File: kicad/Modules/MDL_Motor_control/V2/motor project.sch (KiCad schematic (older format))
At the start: 4 parts

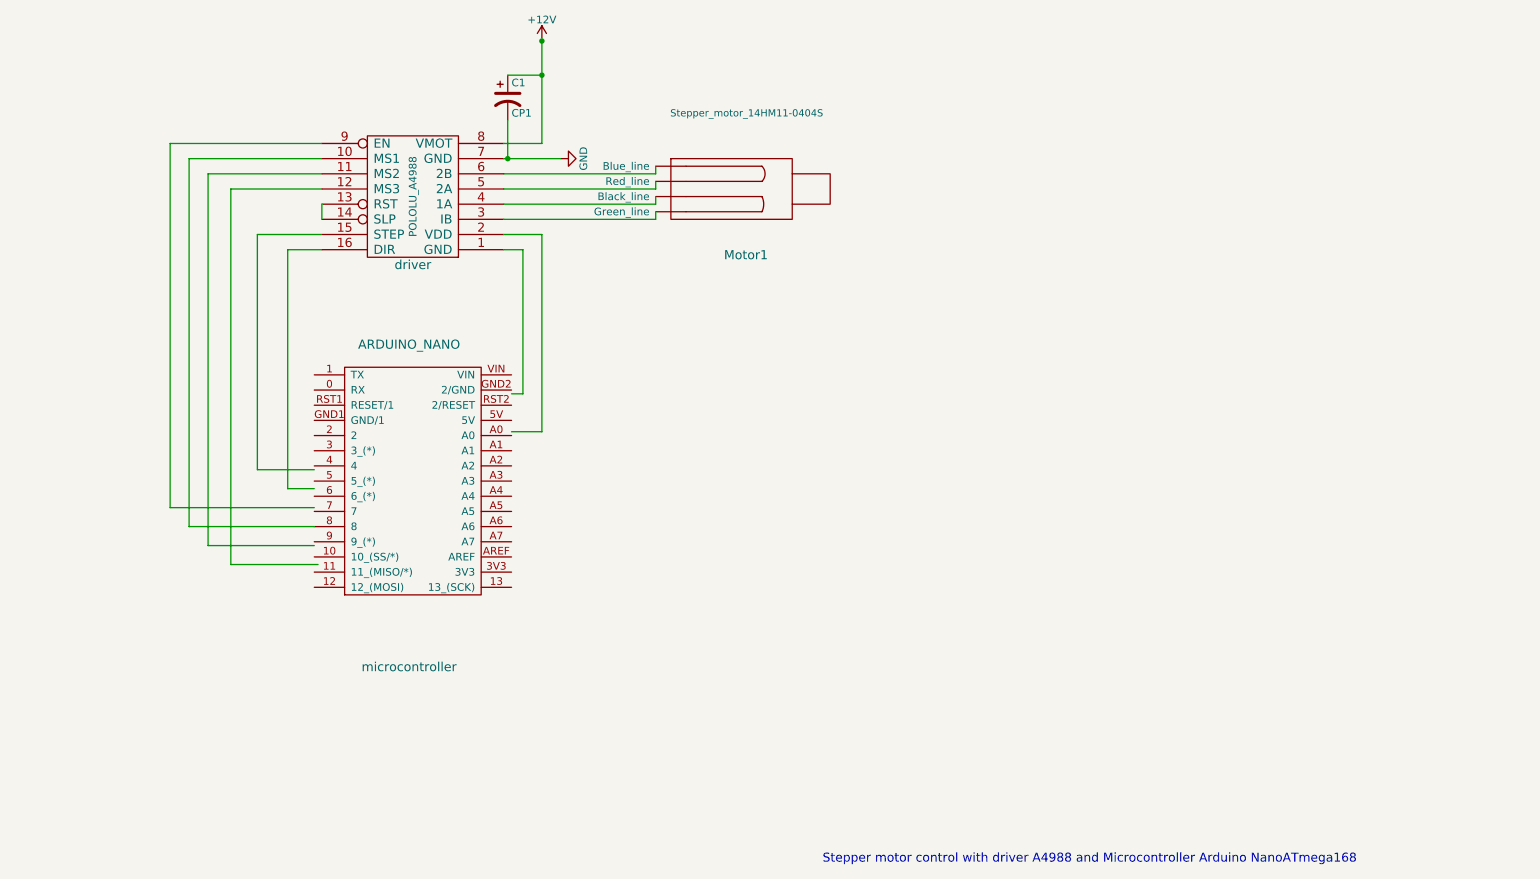
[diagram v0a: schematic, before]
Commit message: adding software modules (flowcharts)
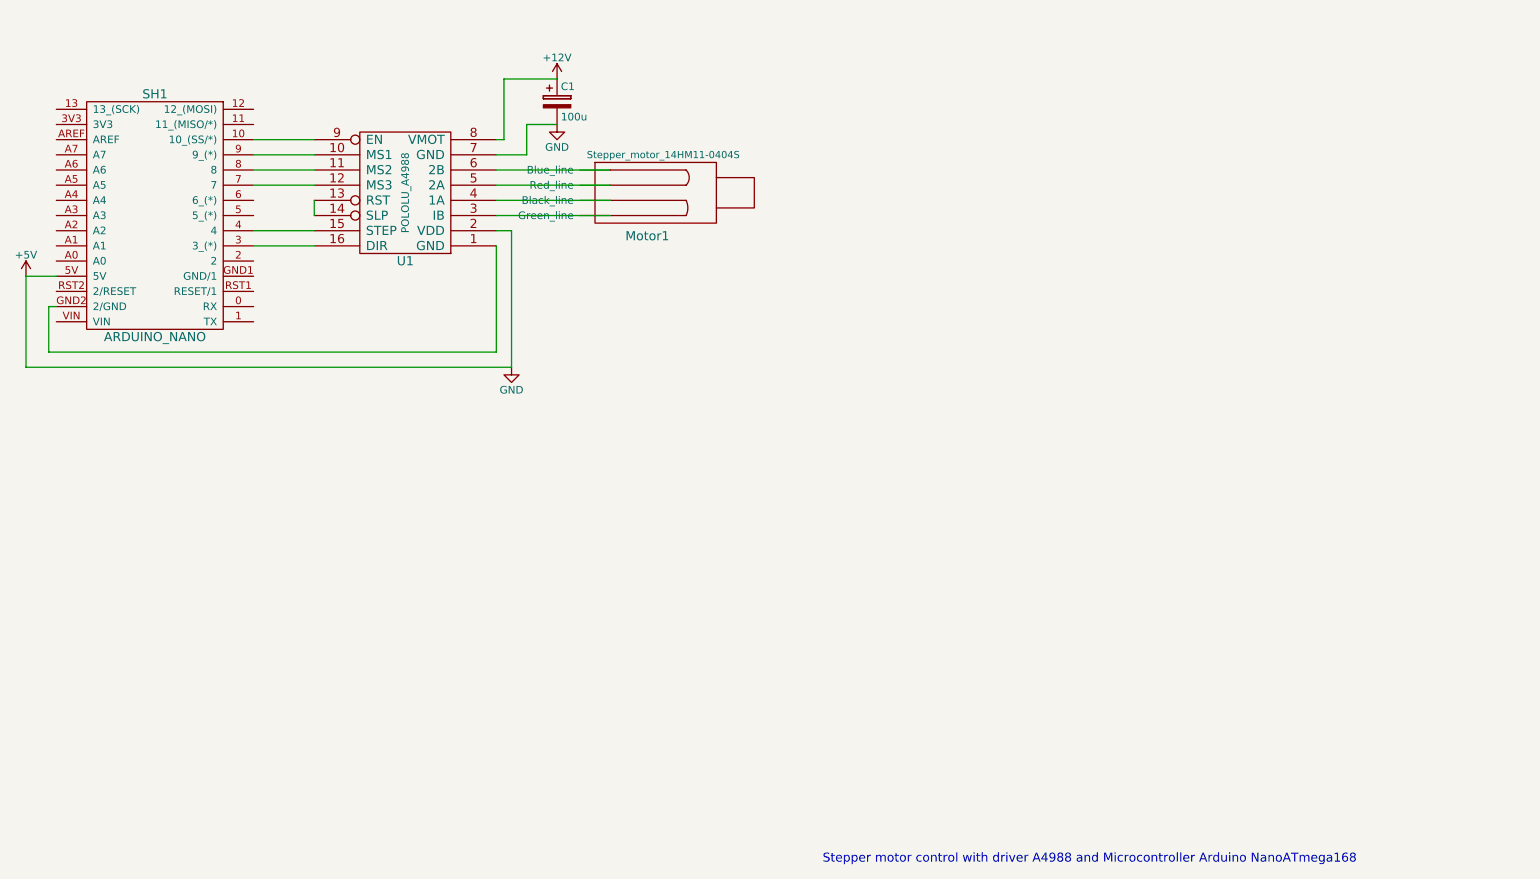
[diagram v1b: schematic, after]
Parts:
- removed C1: CP1, symbol CP1
- removed driver: POLOLU_A4988, symbol POLOLU_A4988
- removed microcontroller: ARDUINO_NANO, symbol ARDUINO_NANO
- added C1: 100u, symbol CP
- added SH1: ARDUINO_NANO, symbol ARDUINO_NANO
- added U1: POLOLU_A4988, symbol POLOLU_A4988
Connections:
- net labels added: +5V
- wire segments 38 -> 26
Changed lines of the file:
@@
 EESchema Schematic File Version 2
-LIBS:pololu_a4988
 LIBS:power
 LIBS:device
@@
 LIBS:contrib
 LIBS:valves
-LIBS:arduino
-LIBS:shield_arduino
-LIBS:stepper_motor_14hm11-0404s
-LIBS:projet moteur-cache
+LIBS:echopen
+LIBS:motor project-cache
 EELAYER 25 0
 EELAYER END
@@
 Comment4 ""
 $EndDescr
+Text Notes 7300 7475 0    59   ~ 0
+Stepper motor control with driver A4988 and Microcontroller Arduino NanoATmega168
 $Comp
-L POLOLU_A4988 driver
-U 1 1 577B8019
-P 4600 3075
-F 0 "driver" H 4600 3525 60  0000 C CNN
-F 1 "POLOLU_A4988" V 4600 3075 50  0000 C CNN
-F 2 "" H 4600 3075 60  0000 C CNN
-F 3 "" H 4600 3075 60  0000 C CNN
-	1    4600 3075
+L POLOLU_A4988 U1
+U 1 1 57A99E63
+P 4550 3050
+F 0 "U1" H 4550 3500 60  0000 C CNN
+F 1 "POLOLU_A4988" V 4550 3050 50  0000 C CNN
+F 2 "" H 4550 3050 60  0000 C CNN
+F 3 "" H 4550 3050 60  0000 C CNN
+	1    4550 3050
 	-1   0    0    1
 $EndComp
 $Comp
-L ARDUINO_NANO microcontroller
-U 1 1 577B8A9A
-P 4600 5100
-F 0 "microcontroller" H 4575 4025 60  0000 C CNN
-F 1 "ARDUINO_NANO" H 4575 6150 60  0000 C CNN
-F 2 "" H 3675 4500 60  0000 C CNN
-F 3 "" H 3675 4500 60  0000 C CNN
-	1    4600 5100
+L ARDUINO_NANO SH1
+U 1 1 57A9ABD4
+P 2900 3050
+F 0 "SH1" H 2900 2400 60  0000 C CNN
+F 1 "ARDUINO_NANO" H 2900 4000 60  0000 C CNN
+F 2 "" H 1975 2450 60  0000 C CNN
+F 3 "" H 1975 2450 60  0000 C CNN
+	1    2900 3050
+	-1   0    0    1
+$EndComp
+$Comp
+L Stepper_motor_14HM11-0404S Motor1
+U 1 1 57A9AFD6
+P 6500 3700
+F 0 "Motor1" H 6000 4100 60  0000 L TNN
+F 1 "Stepper_motor_14HM11-0404S" H 6250 4600 47  0000 C CNN
+F 2 "" H 5800 3600 60  0000 C CNN
+F 3 "" H 5400 5200 60  0000 C CNN
+	1    6500 3700
 	1    0    0    -1
 $EndComp
 Wire Wire Line
-	4000 3425 3775 3425
+	5150 3200 5900 3200
 Wire Wire Line
-	3775 3425 3775 5000
+	5150 3100 5900 3100
 Wire Wire Line
-	3775 5000 3950 5000
+	5150 3000 5900 3000
 Wire Wire Line
-	4000 3325 3575 3325
-Wire Wire Line
-	3575 3325 3575 4875
-Wire Wire Line
-	3575 4875 3950 4875
-Wire Wire Line
-	4000 3225 4000 3125
-Wire Wire Line
-	3400 3025 3400 5500
-Wire Wire Line
-	3400 5500 3975 5500
-Wire Wire Line
-	3250 2925 3250 5375
-Wire Wire Line
-	3125 2825 3125 5250
-Wire Wire Line
-	3000 2725 3000 5125
-Wire Wire Line
-	3000 5125 3950 5125
-Wire Wire Line
-	5200 3425 5325 3425
-Wire Wire Line
-	5325 3425 5325 4375
-Wire Wire Line
-	5325 4375 5250 4375
-Wire Wire Line
-	5200 3325 5450 3325
-Wire Wire Line
-	5450 3325 5450 4625
-Wire Wire Line
-	5450 4625 5250 4625
-Wire Wire Line
-	5200 2925 6200 2925
-Wire Wire Line
-	5200 3125 6200 3125
-Wire Wire Line
-	5200 3225 6200 3225
-Wire Wire Line
-	5200 3025 6200 3025
-Wire Wire Line
-	3125 5250 3950 5250
-Wire Wire Line
-	3250 5375 3950 5375
-Wire Wire Line
-	3400 3025 4000 3025
-Wire Wire Line
-	3250 2925 4000 2925
-Wire Wire Line
-	3125 2825 4000 2825
-Wire Wire Line
-	3000 2725 4000 2725
+	5150 2900 5900 2900
 $Comp
-L +12V #PWR?
-U 1 1 577BC707
-P 5450 2050
-F 0 "#PWR?" H 5450 1900 50  0001 C CNN
-F 1 "+12V" H 5450 2190 50  0000 C CNN
-F 2 "" H 5450 2050 50  0000 C CNN
-F 3 "" H 5450 2050 50  0000 C CNN
-	1    5450 2050
+L CP C1
+U 1 1 57A9B39D
+P 5550 2450
+F 0 "C1" H 5575 2550 50  0000 L CNN
+F 1 "100u" H 5575 2350 50  0000 L CNN
+F 2 "" H 5588 2300 50  0000 C CNN
+F 3 "" H 5550 2450 50  0000 C CNN
+	1    5550 2450
 	1    0    0    -1
 $EndComp
 $Comp
-L GND #PWR?
-U 1 1 577BC727
-P 5575 2825
-F 0 "#PWR?" H 5575 2575 50  0001 C CNN
-F 1 "GND" H 5575 2675 50  0000 C CNN
-F 2 "" H 5575 2825 50  0000 C CNN
-F 3 "" H 5575 2825 50  0000 C CNN
-	1    5575 2825
-	0    -1   -1   0
+L +12V #PWR01
+U 1 1 57A9B43B
+P 5550 2300
+F 0 "#PWR01" H 5550 2150 50  0001 C CNN
+F 1 "+12V" H 5550 2440 50  0000 C CNN
+F 2 "" H 5550 2300 50  0000 C CNN
+F 3 "" H 5550 2300 50  0000 C CNN
+	1    5550 2300
+	1    0    0    -1
 $EndComp
-Wire Wire Line
-	5450 2050 5450 2725
-Wire Wire Line
-	5450 2725 5200 2725
-Connection ~ 5450 2050
-Wire Wire Line
-	5200 2825 5575 2825
 $Comp
-L CP1 C1
-U 1 1 577BC839
-P 5225 2425
-F 0 "C1" H 5250 2525 50  0000 L CNN
-F 1 "CP1" H 5250 2325 50  0000 L CNN
-F 2 "" H 5225 2425 50  0000 C CNN
-F 3 "" H 5225 2425 50  0000 C CNN
-	1    5225 2425
+L GND #PWR02
+U 1 1 57A9B45B
+P 5550 2600
+F 0 "#PWR02" H 5550 2350 50  0001 C CNN
+F 1 "GND" H 5550 2450 50  0000 C CNN
+F 2 "" H 5550 2600 50  0000 C CNN
+F 3 "" H 5550 2600 50  0000 C CNN
+	1    5550 2600
 	1    0    0    -1
 $EndComp
 Wire Wire Line
-	5225 2575 5225 2825
-Connection ~ 5225 2825
+	5150 2800 5350 2800
 Wire Wire Line
-	5225 2275 5450 2275
-Connection ~ 5450 2275
+	5350 2800 5350 2600
 Wire Wire Line
-	6200 2925 6200 2875
+	5350 2600 5550 2600
 Wire Wire Line
-	6200 3025 6200 2975
+	5150 2700 5200 2700
 Wire Wire Line
-	6200 3125 6200 3075
+	5200 2700 5200 2300
 Wire Wire Line
-	6200 3225 6200 3175
-Text Notes 7300 7475 0    59   ~ 0
-Stepper motor control with driver A4988 and Microcontroller Arduino NanoATmega168
+	5200 2300 5550 2300
+Wire Wire Line
+	3550 2700 3950 2700
+Wire Wire Line
+	3550 2800 3950 2800
+Wire Wire Line
+	3550 2900 3950 2900
+Wire Wire Line
+	3550 3000 3950 3000
+Wire Wire Line
+	3950 3100 3950 3200
+Wire Wire Line
+	3550 3300 3950 3300
+Wire Wire Line
+	3550 3400 3950 3400
+Wire Wire Line
+	2250 3800 2200 3800
+Wire Wire Line
+	2200 3800 2200 4100
+Wire Wire Line
+	2200 4100 5150 4100
+Wire Wire Line
+	5150 4100 5150 3400
+Wire Wire Line
+	2250 3600 2050 3600
+Wire Wire Line
+	2050 3600 2050 4200
+Wire Wire Line
+	2050 4200 5250 4200
+Wire Wire Line
+	5250 4200 5250 3300
+Wire Wire Line
+	5250 3300 5150 3300
 $Comp
-L Stepper_motor_14HM11-0404S Motor1
-U 1 1 577BE7D5
-P 7000 3675
-F 0 "Motor1" H 6650 3925 60  0000 L TNN
-F 1 "Stepper_motor_14HM11-0404S" H 6800 4825 47  0000 C CNN
-F 2 "" H 6300 3575 60  0000 C CNN
-F 3 "" H 5900 5175 60  0000 C CNN
-	1    7000 3675
+L +5V #PWR03
+U 1 1 57A9B78D
+P 2050 3600
+F 0 "#PWR03" H 2050 3450 50  0001 C CNN
+F 1 "+5V" H 2050 3740 50  0000 C CNN
+F 2 "" H 2050 3600 50  0000 C CNN
+F 3 "" H 2050 3600 50  0000 C CNN
+	1    2050 3600
 	1    0    0    -1
 $EndComp
+$Comp
+L GND #PWR04
+U 1 1 57A9BA4D
+P 5250 4200
+F 0 "#PWR04" H 5250 3950 50  0001 C CNN
+F 1 "GND" H 5250 4050 50  0000 C CNN
+F 2 "" H 5250 4200 50  0000 C CNN
+F 3 "" H 5250 4200 50  0000 C CNN
+	1    5250 4200
+	1    0    0    -1
+$EndComp
